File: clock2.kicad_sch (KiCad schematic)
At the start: 36 parts, among them CN1 PJ-327A 5JJ, CN2 PJ-327A 5JJ, SW1 SSSS811101, U1 NE555D, U2 NE555D, U3 TC-6615-9.0-160G, U4 NE555D, U5 XL74LS04, U6 XL74LS08, U7 XL74LS32, U8 RM063-105(1M)

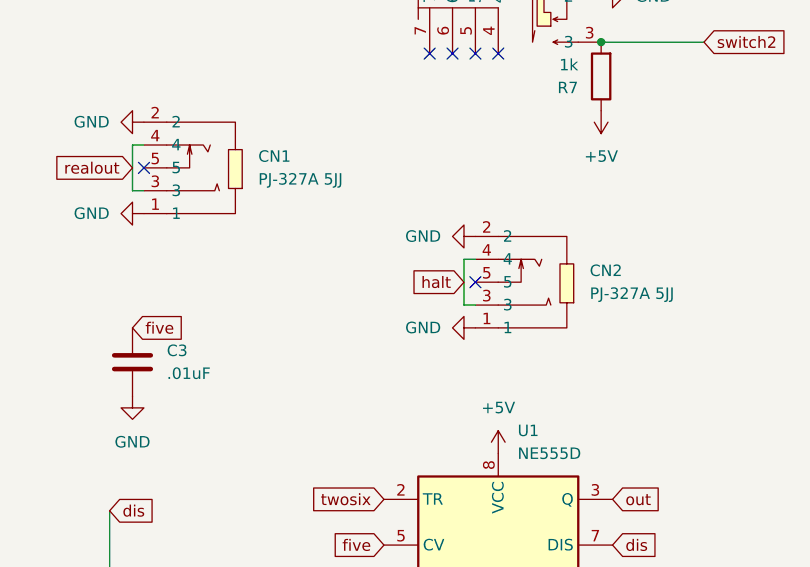
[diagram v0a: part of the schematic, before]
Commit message: use the switching capability of the headphone jack to default the HALT signal to LOW. use resistor to prevent input HALT short to ground before contact breaks
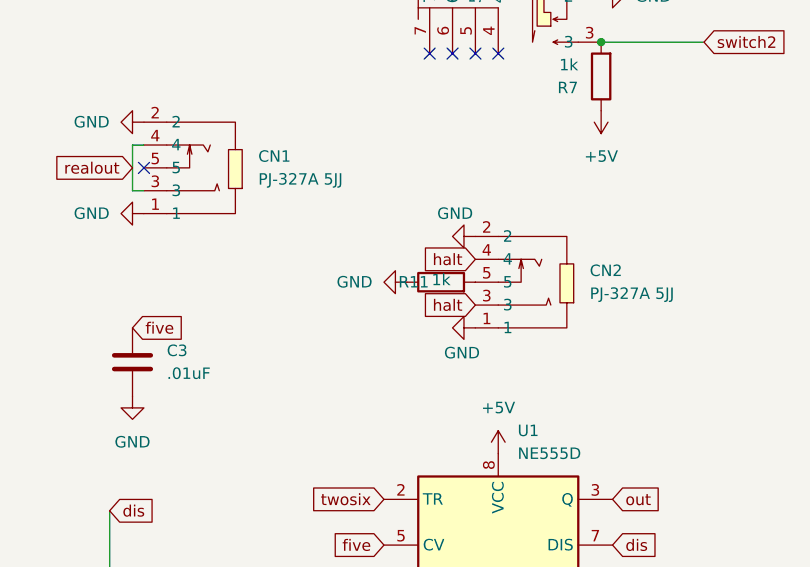
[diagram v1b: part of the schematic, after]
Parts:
- added R11: 1k, Resistor_SMD:R_0805_2012Metric_Pad1.20x1.40mm_HandSolder, symbol Device:R
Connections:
- net GND: now also R11.1
- net at CN2.5: now also R11.2
- no-connect marks 31 -> 30
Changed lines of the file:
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@@
 	)
 	(no_connect
-		(at 137.16 80.01)
-	)
-	(no_connect
 		(at 119.38 36.83)
 	)
@@
 	(wire
 		(pts
-			(xy 135.89 82.55) (xy 135.89 77.47)
-		)
-		(stroke
-			(width 0)
-			(type default)
-		)
-	)
-	(wire
-		(pts
 			(xy 99.06 64.77) (xy 100.33 64.77)
 		)
@@
 	(wire
 		(pts
-			(xy 137.16 82.55) (xy 135.89 82.55)
-		)
-		(stroke
-			(width 0)
-			(type default)
-		)
-	)
-	(wire
-		(pts
 			(xy 107.95 124.46) (xy 107.95 132.08)
 		)
@@
 	(wire
 		(pts
-			(xy 135.89 77.47) (xy 137.16 77.47)
-		)
-		(stroke
-			(width 0)
-			(type default)
-		)
-	)
-	(wire
-		(pts
 			(xy 237.49 138.43) (xy 243.84 138.43)
 		)
@@
 		)
 	)
-	(global_label "halt"
-		(shape input)
-		(at 135.89 80.01 180)
-		(fields_autoplaced yes)
-		(effects
-			(font
-				(size 1.27 1.27)
-			)
-			(justify right)
-		)
-		(property "Intersheetrefs" "${INTERSHEET_REFS}"
-			(at 129.2159 80.01 0)
-			(effects
-				(font
-					(size 1.27 1.27)
-				)
-				(justify right)
-				(hide yes)
-			)
-		)
-	)
 	(global_label "realout"
 		(shape input)
@@
 		)
 	)
+	(global_label "halt"
+		(shape input)
+		(at 137.16 77.47 180)
+		(fields_autoplaced yes)
+		(effects
+			(font
+				(size 1.27 1.27)
+			)
+			(justify right)
+		)
+		(property "Intersheetrefs" "${INTERSHEET_REFS}"
+			(at 130.4859 77.47 0)
+			(effects
+				(font
+					(size 1.27 1.27)
+				)
+				(justify right)
+				(hide yes)
+			)
+		)
+	)
 	(global_label "out3"
 		(shape input)
@@
 		)
 	)
+	(global_label "halt"
+		(shape input)
+		(at 137.16 82.55 180)
+		(fields_autoplaced yes)
+		(effects
+			(font
+				(size 1.27 1.27)
+			)
+			(justify right)
+		)
+		(property "Intersheetrefs" "${INTERSHEET_REFS}"
+			(at 130.4859 82.55 0)
+			(effects
+				(font
+					(size 1.27 1.27)
+				)
+				(justify right)
+				(hide yes)
+			)
+		)
+	)
 	(symbol
 		(lib_id "power:GND")
@@
 		(on_board yes)
 		(dnp no)
-		(fields_autoplaced yes)
 		(property "Reference" "#PWR038"
 			(at 130.81 74.93 0)
@@
 		)
 		(property "Value" "GND"
-			(at 133.35 74.9299 90)
+			(at 136.906 72.39 90)
 			(effects
 				(font
@@
 	)
 	(symbol
+		(lib_id "Device:R")
+		(at 133.35 80.01 90)
+		(unit 1)
+		(exclude_from_sim no)
+		(in_bom yes)
+		(on_board yes)
+		(dnp no)
+		(property "Reference" "R11"
+			(at 130.302 80.01 90)
+			(effects
+				(font
+					(size 1.27 1.27)
+				)
+			)
+		)
+		(property "Value" "1k"
+			(at 133.35 79.756 90)
+			(effects
+				(font
+					(size 1.27 1.27)
+				)
+			)
+		)
+		(property "Footprint" "Resistor_SMD:R_0805_2012Metric_Pad1.20x1.40mm_HandSolder"
+			(at 133.35 81.788 90)
+			(effects
+				(font
+					(size 1.27 1.27)
+				)
+				(hide yes)
+			)
+		)
+		(property "Datasheet" "~"
+			(at 133.35 80.01 0)
+			(effects
+				(font
+					(size 1.27 1.27)
+				)
+				(hide yes)
+			)
+		)
+		(property "Description" "Resistor"
+			(at 133.35 80.01 0)
+			(effects
+				(font
+					(size 1.27 1.27)
+				)
+				(hide yes)
+			)
+		)
+		(pin "1"
+		)
+		(pin "2"
+		)
+		(instances
+			(project "clock2"
+				(path "/bfb0fb97-0177-4e63-ba26-052e73c1a407"
+					(reference "R11")
+					(unit 1)
+				)
+			)
+		)
+	)
+	(symbol
 		(lib_id "power:GND")
 		(at 110.49 154.94 90)
@@
 		(on_board yes)
 		(dnp no)
-		(fields_autoplaced yes)
 		(property "Reference" "#PWR039"
 			(at 130.81 85.09 0)
@@
 		)
 		(property "Value" "GND"
-			(at 133.35 85.0899 90)
+			(at 137.668 87.884 90)
 			(effects
 				(font
@@
 					(unit 1)
 				)
+			)
+		)
+	)
+	(symbol
+		(lib_id "power:GND")
+		(at 129.54 80.01 270)
+		(unit 1)
+		(exclude_from_sim no)
+		(in_bom yes)
+		(on_board yes)
+		(dnp no)
+		(fields_autoplaced yes)
+		(property "Reference" "#PWR040"
+			(at 123.19 80.01 0)
+			(effects
+				(font
+					(size 1.27 1.27)
+				)
+				(hide yes)
+			)
+		)
+		(property "Value" "GND"
+			(at 125.73 80.0099 90)
+			(effects
+				(font
+					(size 1.27 1.27)
+				)
+				(justify right)
+			)
+		)
+		(property "Footprint" ""
+			(at 129.54 80.01 0)
+			(effects
+				(font
+					(size 1.27 1.27)
+				)
+				(hide yes)
+			)
+		)
+		(property "Datasheet" ""
+			(at 129.54 80.01 0)
+			(effects
+				(font
+					(size 1.27 1.27)
+				)
+				(hide yes)
+			)
+		)
+		(property "Description" "Power symbol creates a global label with name \"GND\" , ground"
+			(at 129.54 80.01 0)
+			(effects
+				(font
+					(size 1.27 1.27)
+				)
+				(hide yes)
+			)
+		)
+		(pin "1"
+		)
+		(instances
+			(project "clock2"
+				(path "/bfb0fb97-0177-4e63-ba26-052e73c1a407"
+					(reference "#PWR040")
+					(unit 1)
+				)

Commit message: v1 finalized
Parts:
- C1: footprint Capacitor_SMD:C_0805_2012Metric_Pad1.18x1.45mm_HandSolder -> easyeda2kicad:C0805; symbol Device:C -> easyeda2kicad:CL21B105KBFNNNE; LCSC Part (none) -> C28323
- C2, C4: footprint Capacitor_SMD:C_0805_2012Metric_Pad1.18x1.45mm_HandSolder -> easyeda2kicad:C0805; symbol Device:C -> easyeda2kicad:CC0805KRX7R9BB104; LCSC Part (none) -> C49678
- C3, C5, C6: footprint Capacitor_SMD:C_0805_2012Metric_Pad1.18x1.45mm_HandSolder -> easyeda2kicad:C0805; symbol Device:C -> easyeda2kicad:CC0805KRX7R9BB103; LCSC Part (none) -> C83170
- R1, R11, R2, R4, R6, R7: footprint Resistor_SMD:R_0805_2012Metric_Pad1.20x1.40mm_HandSolder -> easyeda2kicad:R0805; symbol Device:R -> easyeda2kicad:RC0805FR-071KL; LCSC Part (none) -> C95781
- R10, R3, R8, R9: footprint Resistor_SMD:R_0805_2012Metric_Pad1.20x1.40mm_HandSolder -> easyeda2kicad:R0805; symbol Device:R -> easyeda2kicad:0805W8F2200T5E; LCSC Part (none) -> C17557
- R5: footprint Resistor_SMD:R_0805_2012Metric_Pad1.20x1.40mm_HandSolder -> easyeda2kicad:R0805; symbol Device:R -> easyeda2kicad:RC0805FR-071ML; LCSC Part (none) -> C107700
- U1, U2, U4: footprint Package_SO:SOIC-8_3.9x4.9mm_P1.27mm -> easyeda2kicad:SOIC-8_L4.9-W3.9-P1.27-LS6.0-BL; symbol Timer:NE555D -> easyeda2kicad:NE555DR; LCSC Part (none) -> C7593
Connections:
- net +5V: now also C2.2, R1.2, R4.2, R5.1, R6.2, R7.2; no longer C2.1, R1.1, R4.1, R5.2, R6.1, R7.1
- net GND: now also C1.2, C2.1, C3.1, C4.1, C5.1, C6.1, R10.2, R11.2, R3.2, R8.2, R9.2; no longer C1.1, C2.2, C3.2, C4.2, C5.2, C6.2, R10.1, R11.1, R3.1, R8.1, R9.1
- net button: now also R4.1; no longer R4.2
- net dis: now also R1.1; no longer R1.2
- net dis2: now also C4.2, R5.2; no longer C4.1, R5.1
- net five: now also C3.2; no longer C3.1
- net five2: now also C5.2; no longer C5.1
- net five3: now also C6.2; no longer C6.1
- net halt: now also U5.3 (2A); no longer U5.9 (4A)
- net haltbar: now also U5.4 (2Y); no longer U5.8 (4Y)
- net switch: now also R6.1; no longer R6.2
- net switch2: now also R7.1; no longer R7.2
- net twosix: now also C1.1; no longer C1.2
- net at D3.1 (K): now also R9.1; no longer R9.2
- net at CN2.5: now also R11.1; no longer R11.2
- net at D4.1 (K): now also R10.1; no longer R10.2
- net at D1.1 (K): now also R3.1; no longer R3.2
- net at D2.1 (K): now also R8.1; no longer R8.2
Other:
- note added: "555 Pin 5's"
- note added: "AND"
- note added: "Astable 555"
- note added: "Bistable 555"
- note added: "DC Jack and Decoupling"
- note added: "Halt headphone jack"
- note added: "Logic"
- note added: "Monostable 555"
- note added: "NOT"
- note added: "OR"
- note added: "Output LEDs"
- note added: "Output jack"
- moved on the sheet: CN1, CN2, DC1, H1, H2, H3, H4, SW1, U3, U5, U6, U8
